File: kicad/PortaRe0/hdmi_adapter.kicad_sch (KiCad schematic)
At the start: 2 parts, among them J5 Conn_02x08_Odd_Even

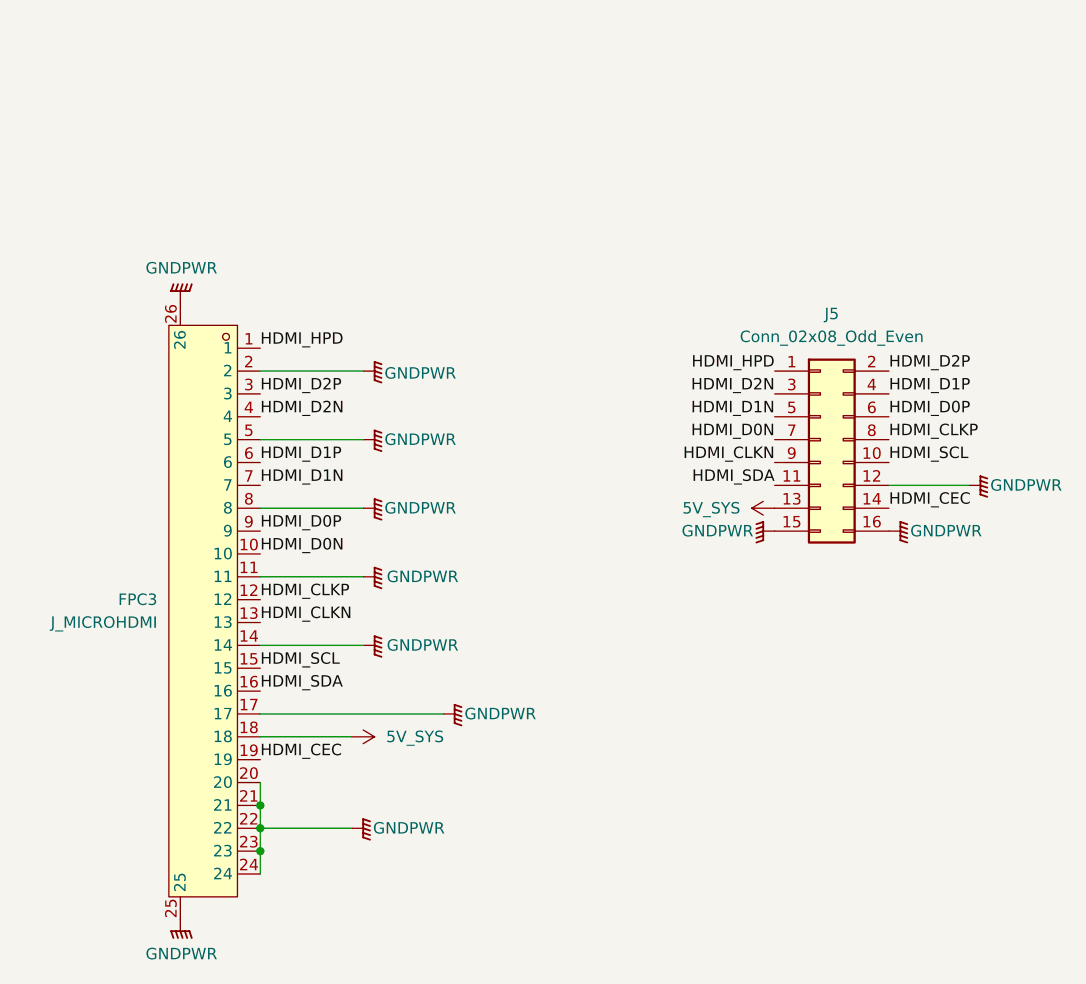
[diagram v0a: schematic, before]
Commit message: KiCad: usb_adapterシート新設・connectorsシート整理
- usb_adapter.kicad_sch 新設（J_SBC_USB1/J_SBC_USB2を移動）
- FPCテール直挿し方式採用（中間コネクタなし）
- FPC 24pin ピン割り当て確定（差動ペア間GND配置）
- connectorsシートにC2856805（ZIF）×2追加
- .gitignore: kicad/PDF/ を除外に追加

Co-Authored-By: Claude Sonnet 4.6 <noreply@anthropic.com>
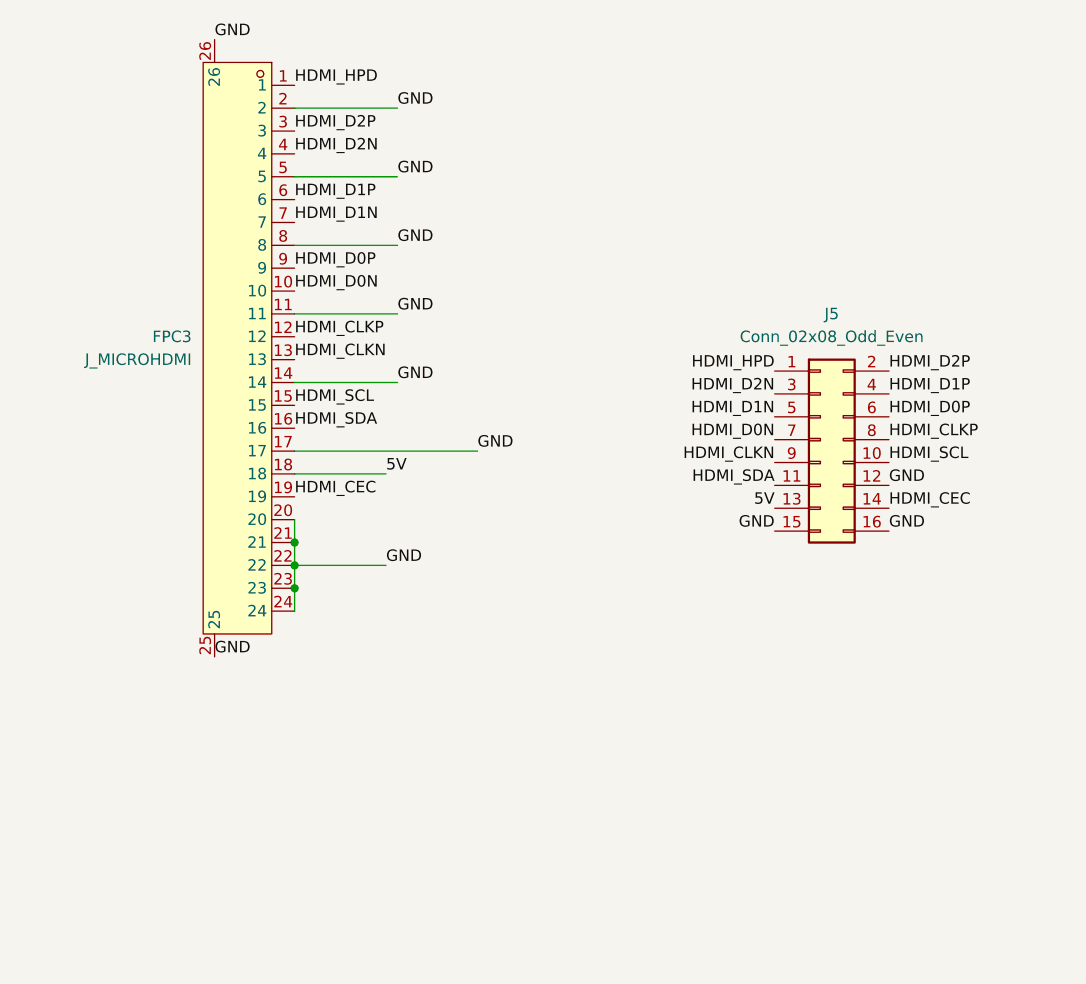
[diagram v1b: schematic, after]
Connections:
- net 5V_SYS renamed 5V
- net GNDPWR renamed GND
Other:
- moved on the sheet: FPC3

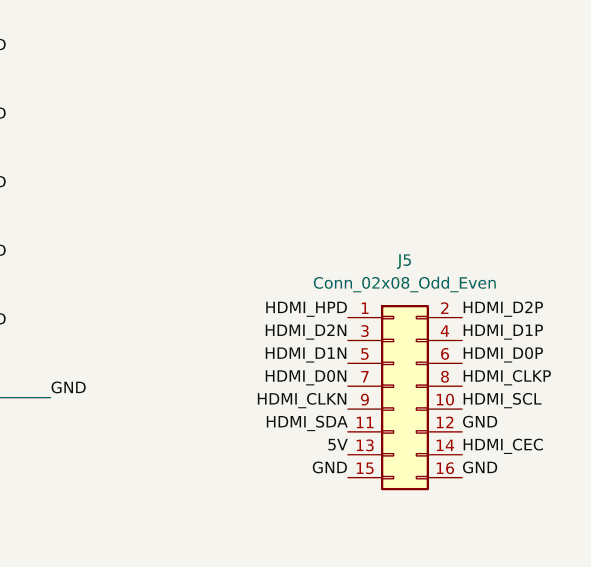
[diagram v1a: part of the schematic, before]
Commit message: KiCad/Docs: session30終了処理・フットプリント割り当て完了・コネクタ確定
- フットプリント全割り当て完了（全シート）
- 新規フットプリント追加: SKSCLBE010/SKRPABE010/クリスタル/インダクタ×3/JST PHコネクタ×2
- コネクタ確定: バッテリー=B8B-PH-K-S(C157974) / SPK+FAN=B2B-PH-K-S(C131337)
- J5(hdmi_adapter): PinHeader_2x08_P2.00mm_Vertical
- Claude.md: ファン制御 RP2040 #1 GP26→BSS138→J6 に更新
- passive_parts.txt: コネクタセクション追加

Co-Authored-By: Claude Sonnet 4.6 <noreply@anthropic.com>
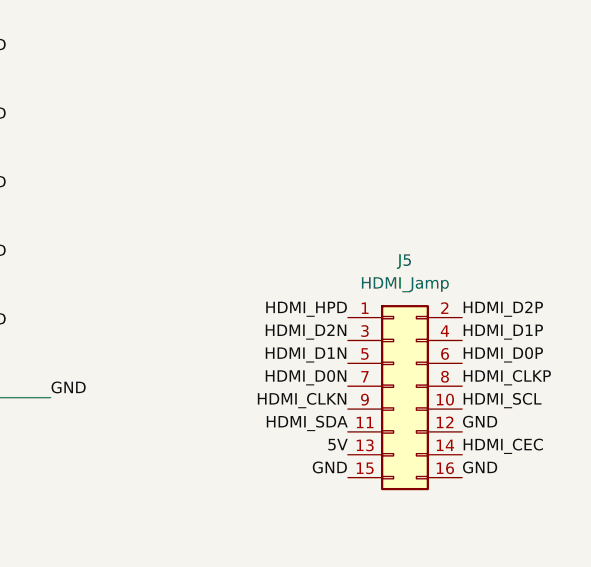
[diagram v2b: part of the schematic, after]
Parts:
- J5: value Conn_02x08_Odd_Even -> HDMI_Jamp; footprint (none) -> Connector_PinHeader_2.00mm:PinHeader_2x08_P2.00mm_Vertical
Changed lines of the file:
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@@
 			)
 		)
-		(property "Value" "Conn_02x08_Odd_Even"
+		(property "Value" "HDMI_Jamp"
 			(at 120.65 53.34 0)
 			(effects
@@
 			)
 		)
-		(property "Footprint" ""
+		(property "Footprint" "Connector_PinHeader_2.00mm:PinHeader_2x08_P2.00mm_Vertical"
 			(at 119.38 64.77 0)
 			(effects
